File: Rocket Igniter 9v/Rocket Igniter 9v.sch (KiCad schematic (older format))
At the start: 25 parts, among them J1 1711725, J2 1711725, K1 G5Q-1 DC5, Q1 BC327, Q2 PN2222ABU, SW1 Y201132C203NQ, SW2 M2011S3S1W01, SW3 RP3502ARED

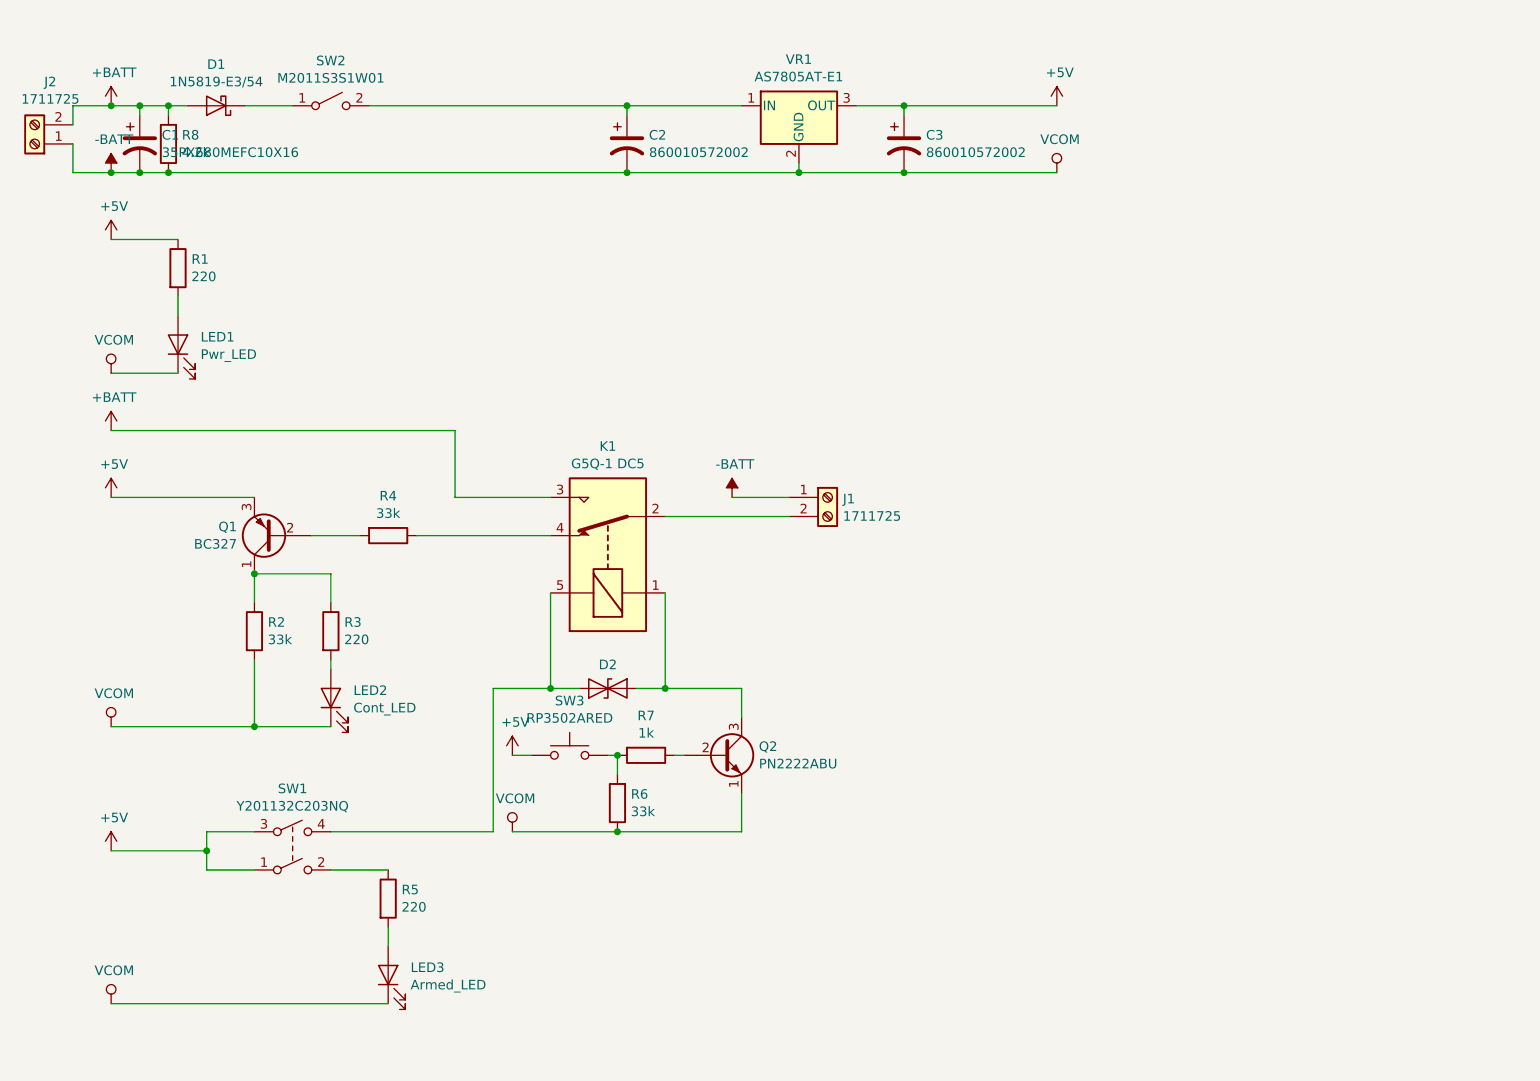
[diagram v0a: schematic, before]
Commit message: clean up schematic
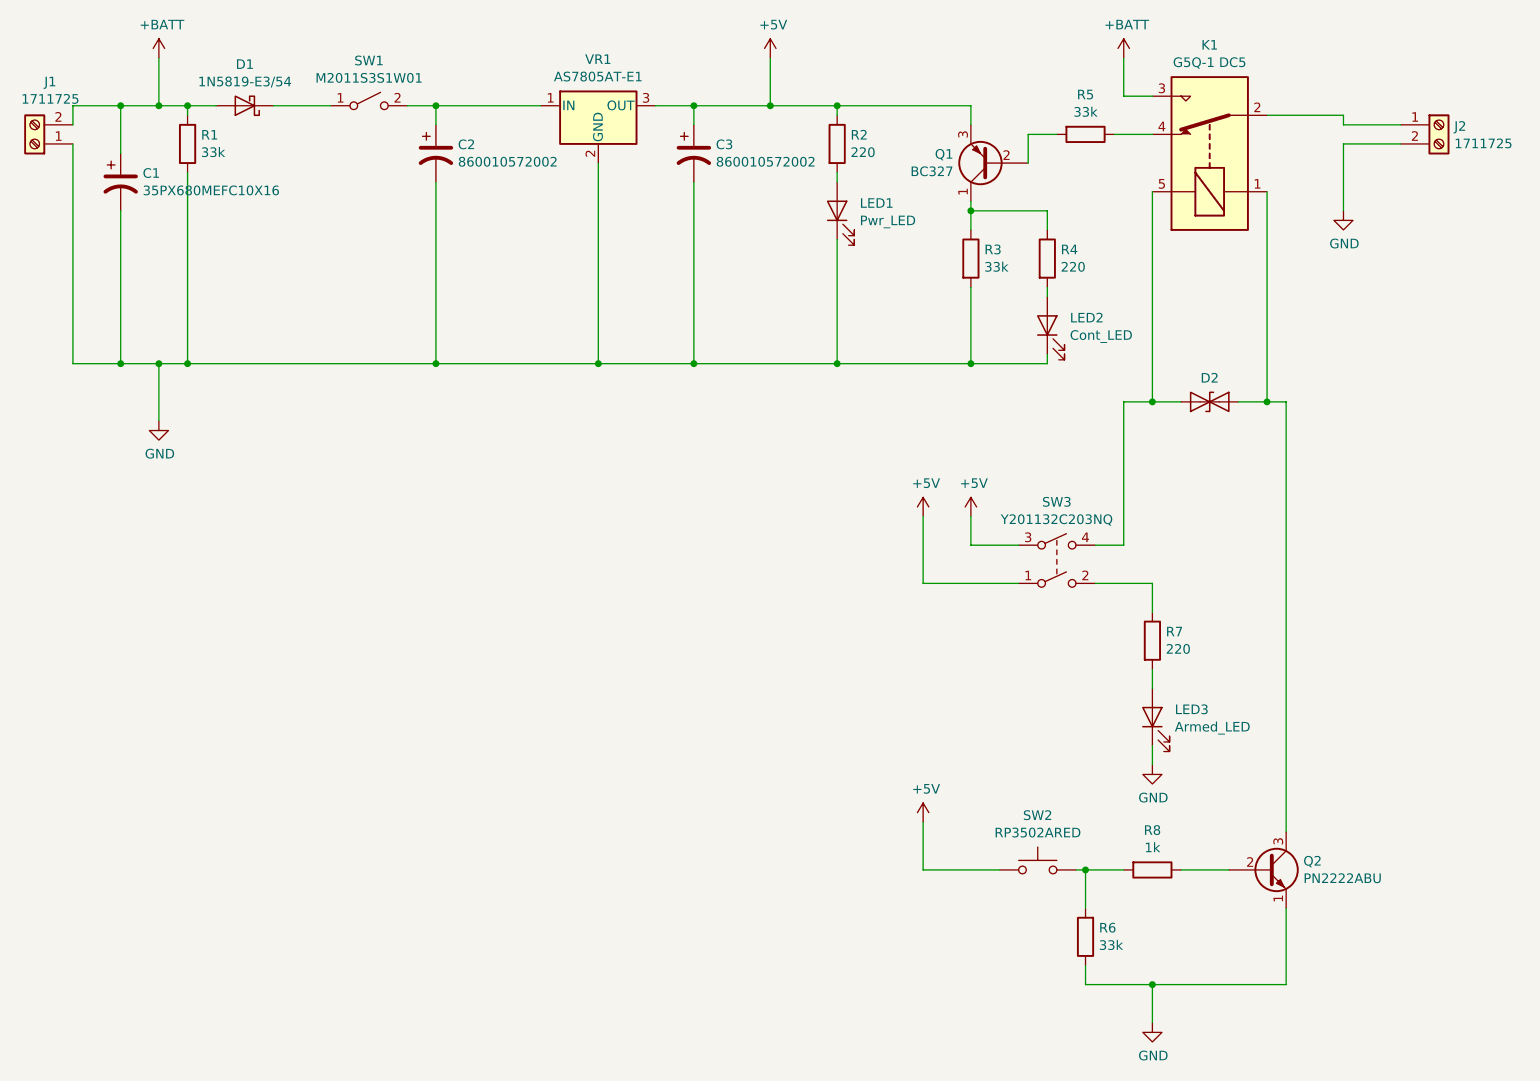
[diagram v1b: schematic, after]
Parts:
- removed R5: 220, Resistor_THT:R_Axial_DIN0207_L6.3mm_D2.5mm_P10.16mm_Horizontal, symbol Device:R
- removed SW1: Y201132C203NQ, Connector_Wire:SolderWirePad_2x02_P5.08mm_Drill1.5mm, symbol Switch:SW_DPST
- removed SW3: RP3502ARED, Connector_Wire:SolderWirePad_1x02_P5.08mm_Drill1.5mm, symbol Switch:SW_Push
- added R8: 1k, Resistor_THT:R_Axial_DIN0207_L6.3mm_D2.5mm_P10.16mm_Horizontal, symbol Device:R
- added SW2: RP3502ARED, Connector_Wire:SolderWirePad_1x02_P5.08mm_Drill1.5mm, symbol Switch:SW_Push
- added SW3: Y201132C203NQ, Connector_Wire:SolderWirePad_2x02_P5.08mm_Drill1.5mm, symbol Switch:SW_DPST
- C1: Part (none) -> 35PX680MEFC10X16; Spice_Model (none) -> 680u; Spice_Netlist_Enabled (none) -> Y; Spice_Primitive (none) -> C
- D1: Part (none) -> 1N5819-E3/54; Spice_Model (none) -> 1N5819-E3/54; Spice_Netlist_Enabled (none) -> Y; Spice_Primitive (none) -> D
- R1: renamed from R8; value 4.2k -> 33k; Spice_Model (none) -> 33k; Spice_Netlist_Enabled (none) -> Y; Spice_Primitive (none) -> R
- R7: value 1k -> 220
- renumbered J2 to J1, J1 to J2, R1 to R2, R2 to R3, R3 to R4, R4 to R5, SW2 to SW1
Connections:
- net +5V: now also SW2.1, SW3.1, SW3.3
- net at K1.2: now also J2.1 (Pin_1); no longer J2.2 (Pin_2)
- net at D2.1 (A1), K1.5: now also SW3.4
- net at LED3.2 (A): now also R7.2
- net at R7.1: now also SW3.2; no longer Q2.2 (B)
- net at R6.2: now also R8.2, SW2.2; no longer R7.2
- net -BATT renamed GND
- net GND: now also J2.2 (Pin_2); no longer J2.1 (Pin_1)
- new net: Q2.2 (B), R8.1
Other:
- moved on the sheet: C1, C2, C3, D1, J2, K1, LED1, LED2, Q1, R1, R2, R3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
